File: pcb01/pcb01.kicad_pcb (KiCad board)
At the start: 2 copper layers, 118.1 x 98.4 mm, 38 parts, among them J1 DIN41612_02x32_AC, J10 Conn_01x02_Socket, J11 Conn_01x09, J2 Data Bus, J3 Address Bus, J4 Display, J5 UART, J6 UART_IRQ, J7 Jmp_Irq, J8 Jmp_NMI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

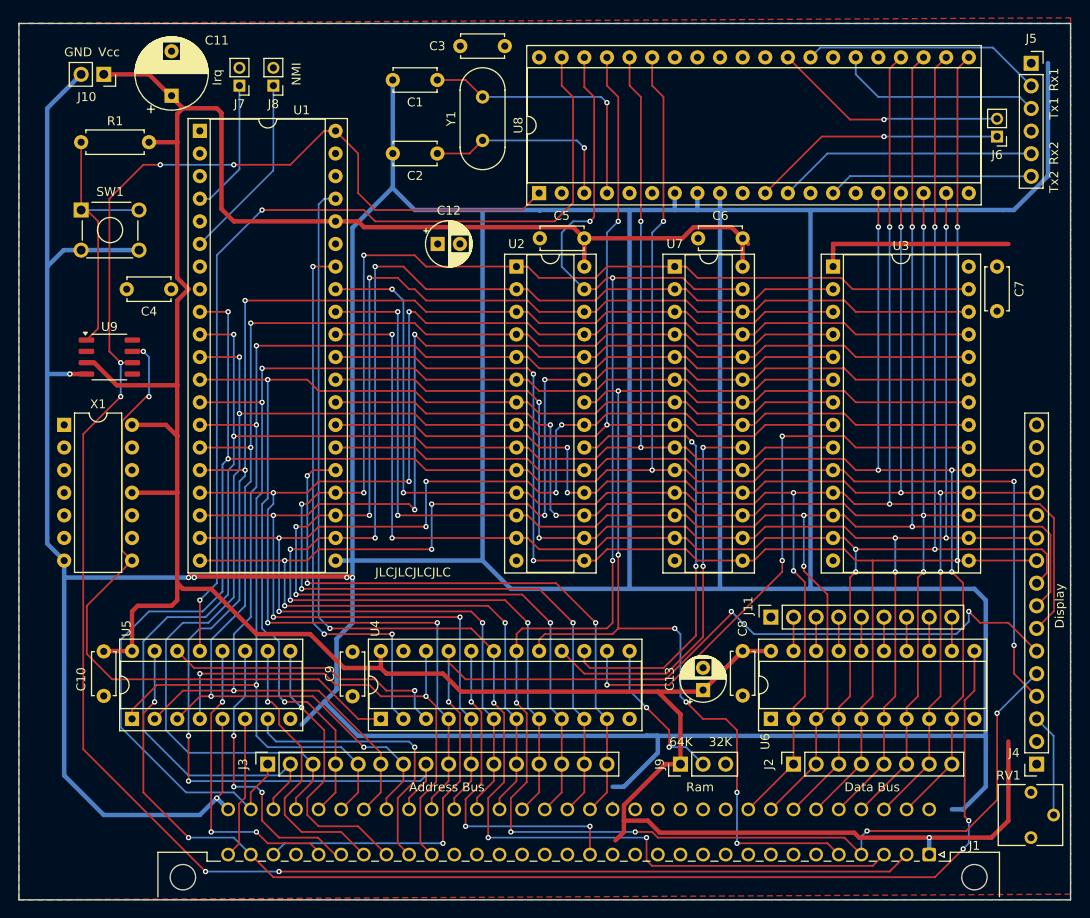
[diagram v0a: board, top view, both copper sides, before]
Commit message: add gpio00 leds
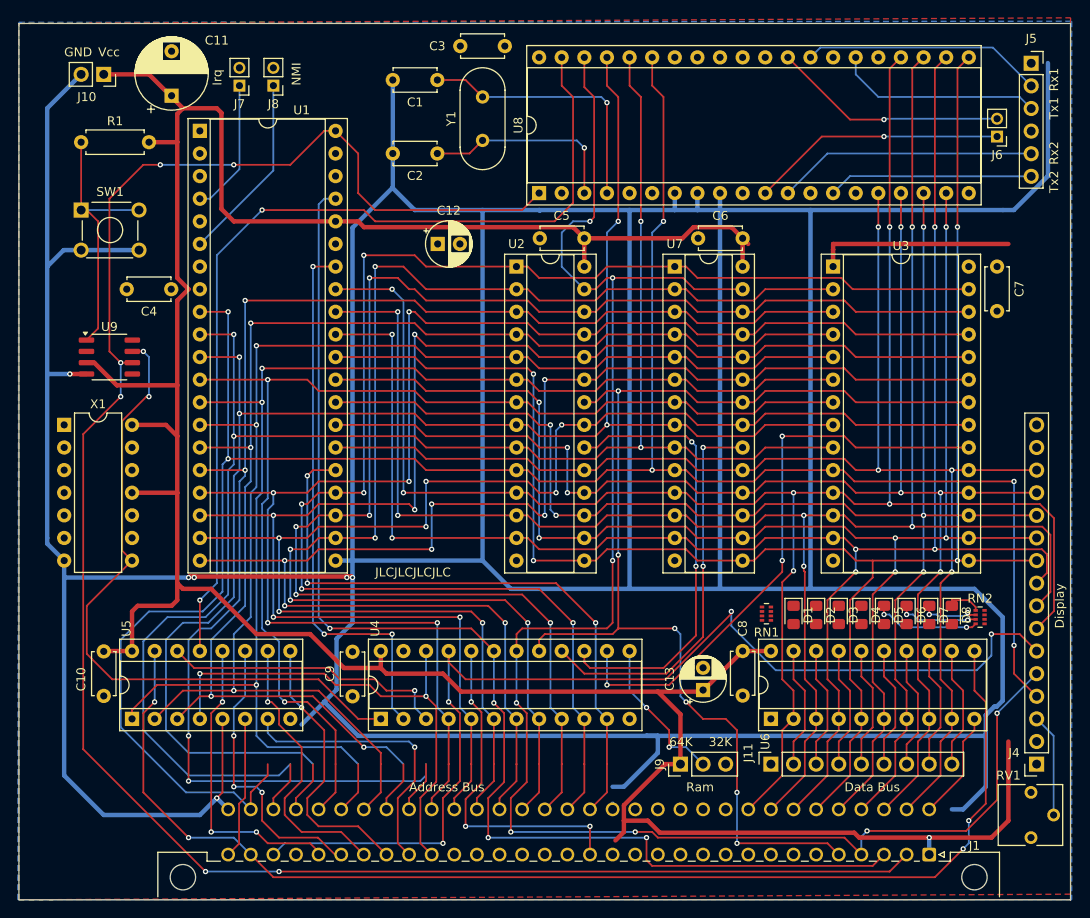
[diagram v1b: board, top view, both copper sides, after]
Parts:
- removed J2: Data Bus, Connector_PinSocket_2.54mm:PinSocket_1x08_P2.54mm_Vertical
- removed J3: Address Bus, Connector_PinSocket_2.54mm:PinSocket_1x16_P2.54mm_Vertical
- added D1: LED_Small, LED_SMD:LED_0805_2012Metric_Pad1.15x1.40mm_HandSolder, F.Cu at (108.6, 86.1)
- added D2: LED_Small, LED_SMD:LED_0805_2012Metric_Pad1.15x1.40mm_HandSolder, F.Cu at (111.1, 86.1)
- added D3: LED_Small, LED_SMD:LED_0805_2012Metric_Pad1.15x1.40mm_HandSolder, F.Cu at (113.7, 86.1)
- added D4: LED_Small, LED_SMD:LED_0805_2012Metric_Pad1.15x1.40mm_HandSolder, F.Cu at (116.2, 86.1)
- added D5: LED_Small, LED_SMD:LED_0805_2012Metric_Pad1.15x1.40mm_HandSolder, F.Cu at (118.7, 86.1)
- added D6: LED_Small, LED_SMD:LED_0805_2012Metric_Pad1.15x1.40mm_HandSolder, F.Cu at (121.3, 86.1)
- added D7: LED_Small, LED_SMD:LED_0805_2012Metric_Pad1.15x1.40mm_HandSolder, F.Cu at (123.8, 86.1)
- added D8: LED_Small, LED_SMD:LED_0805_2012Metric_Pad1.15x1.40mm_HandSolder, F.Cu at (126.4, 86.1)
- added RN1: R_Pack04, Resistor_SMD:R_Array_Concave_4x0402, F.Cu at (105.5, 86.0)
- added RN2: R_Pack04, Resistor_SMD:R_Array_Concave_4x0402, F.Cu at (129.5, 86.4)
- RV1: value R_Potentiometer_Small -> R_LCD_BIAS
- moved J11 16.5 mm to (106.0, 102.9)
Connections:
- net Net-(J11-Pin_2) renamed /GPIO00_O0
- net Net-(J11-Pin_3) renamed /GPIO00_O1
- net Net-(J11-Pin_4) renamed /GPIO00_O2
- net Net-(J11-Pin_5) renamed /GPIO00_O3
- net Net-(J11-Pin_6) renamed /GPIO00_O4
- net Net-(J11-Pin_7) renamed /GPIO00_O5
- net Net-(J11-Pin_8) renamed /GPIO00_O6
- net Net-(J11-Pin_9) renamed /GPIO00_O7
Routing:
- net GND: track 685.4 -> 699.4 mm
- net Net-(D5-K): track 0.00 -> 12.0 mm, vias 0 -> 2
- net /GPIO00_O7: track 3.81 -> 13.8 mm
- net /GPIO00_O0: track 3.81 -> 13.8 mm
- net /GPIO00_O5: track 3.81 -> 13.8 mm
- net /GPIO00_O2: track 3.81 -> 13.8 mm
- net /GPIO00_O1: track 3.81 -> 13.8 mm
- net /GPIO00_O6: track 3.81 -> 13.8 mm
- net /GPIO00_O4: track 3.81 -> 13.8 mm
- net /GPIO00_O3: track 3.81 -> 13.8 mm
- net Net-(D6-K): track 0.00 -> 9.03 mm, vias 0 -> 2
- net Net-(D7-K): track 0.00 -> 6.52 mm, vias 0 -> 2
- net Net-(D8-K): track 0.00 -> 4.01 mm
- net /DISP_EN: track 118.5 -> 121.5 mm
- net /D1: track 204.8 -> 203.7 mm
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
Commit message: wire up GPIO0 leds, adapt design rules
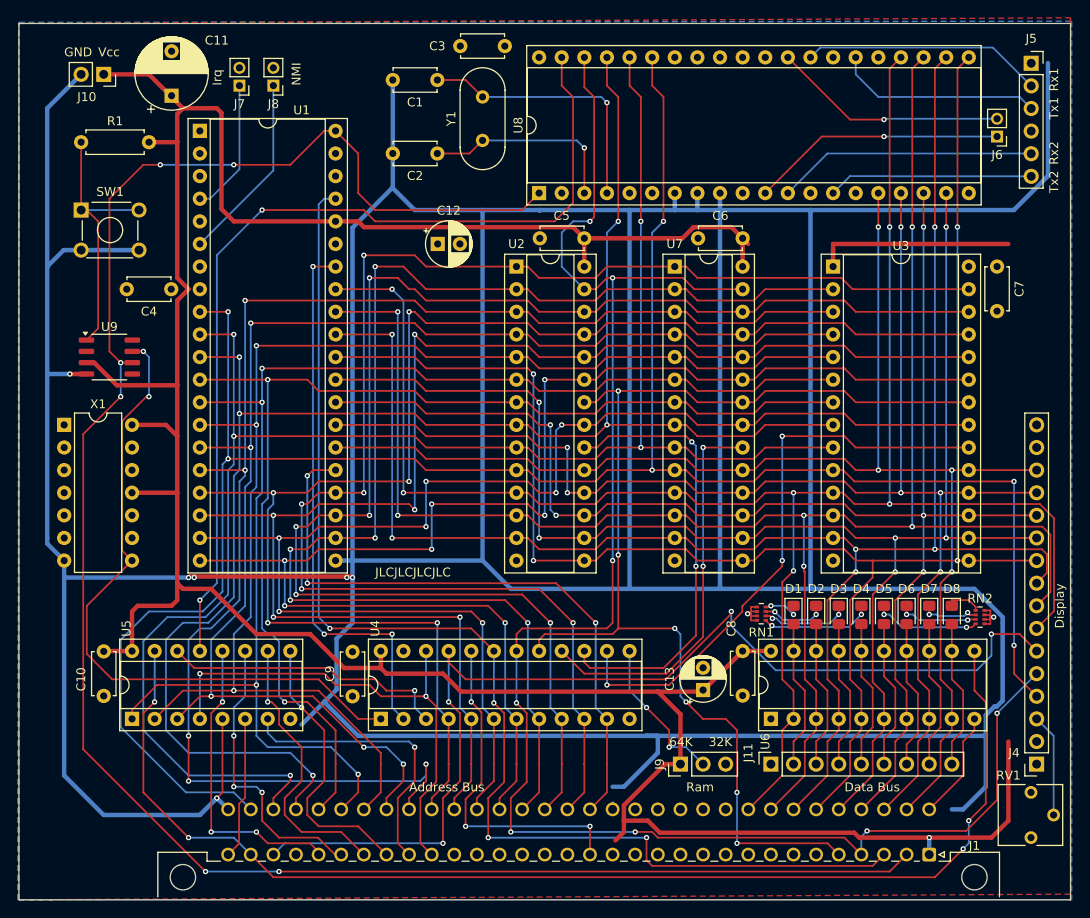
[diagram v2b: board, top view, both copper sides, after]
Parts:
- moved RN1 0.58 mm to (105.0, 86.0)
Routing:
- net Net-(D4-K): track 0.00 -> 12.6 mm, vias 0 -> 2
- net Net-(D3-K): track 0.00 -> 9.94 mm, vias 0 -> 2
- net GND: track 699.4 -> 708.4 mm, vias 6 -> 8
- net Net-(D2-K): track 0.00 -> 7.27 mm, vias 0 -> 2
- net /A0: track 246.7 -> 240.8 mm
- net Net-(D1-K): track 0.00 -> 4.56 mm, vias 0 -> 2
- net /GPIO00_O7: track 13.8 -> 16.8 mm
- net /GPIO00_O6: track 13.8 -> 16.8 mm
- net /GPIO00_O5: track 13.8 -> 16.8 mm
- net /GPIO00_O4: track 13.8 -> 16.8 mm
- net /GPIO00_O3: track 13.8 -> 16.8 mm
- net /GPIO00_O2: track 13.8 -> 16.8 mm
- net /GPIO00_O1: track 13.8 -> 16.8 mm
- net /GPIO00_O0: track 13.8 -> 16.8 mm
- net /A1: track 194.3 -> 192.5 mm, vias 4 -> 5
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
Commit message: kind of final pcb design
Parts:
- added D10: LED_Small, LED_SMD:LED_0805_2012Metric_Pad1.15x1.40mm_HandSolder, F.Cu at (86.4, 101.6)
- added D11: LED_Small, LED_SMD:LED_0805_2012Metric_Pad1.15x1.40mm_HandSolder, F.Cu at (83.8, 101.6)
- added D12: LED_Small, LED_SMD:LED_0805_2012Metric_Pad1.15x1.40mm_HandSolder, F.Cu at (81.3, 101.6)
- added D9: LED_Small, LED_SMD:LED_0805_2012Metric_Pad1.15x1.40mm_HandSolder, F.Cu at (88.9, 101.6)
- added RN3: R_Pack04, Resistor_SMD:R_Array_Concave_4x0402, B.Cu at (85.0, 105.0)
- RN1, RN2: moved to B.Cu
- moved D4 7.70 mm to (108.5, 86.1)
- moved D1 7.62 mm to (116.2, 86.1)
- moved D5 7.62 mm to (126.4, 86.1)
- moved D8 7.62 mm to (118.7, 86.1)
- moved D2 2.54 mm to (113.7, 86.1)
- moved D3 2.54 mm to (111.1, 86.1)
- moved D6 2.54 mm to (123.8, 86.1)
- moved D7 2.54 mm to (121.3, 86.1)
- moved RN2 0.64 mm to (128.9, 86.2)
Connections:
- D1 pad 2: /GPIO00_O0 -> /GPIO00_O3
- D2 pad 2: /GPIO00_O1 -> /GPIO00_O2
- D3 pad 2: /GPIO00_O2 -> /GPIO00_O1
- D4 pad 2: /GPIO00_O3 -> /GPIO00_O0
- D5 pad 2: /GPIO00_O4 -> /GPIO00_O7
- D6 pad 2: /GPIO00_O5 -> /GPIO00_O6
- D7 pad 2: /GPIO00_O6 -> /GPIO00_O5
- D8 pad 2: /GPIO00_O7 -> /GPIO00_O4
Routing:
- net /~{CS_RAM0}: track 50.4 -> 61.3 mm, vias 2 -> 3
- net /~{CS_RAM1}: track 44.3 -> 55.3 mm, vias 2 -> 3
- net Net-(D5-K): track 12.0 -> 2.30 mm, vias 2 -> 1
- net GND: track 708.4 -> 699.9 mm, vias 8 -> 6
- net Net-(D4-K): track 12.6 -> 4.44 mm, vias 2 -> 1
- net Net-(D1-K): track 4.56 -> 12.6 mm, vias 2 -> 1
- net /~{QWE_RAM}: track 197.9 -> 205.7 mm
- net /~{CS_ROM}: track 65.5 -> 72.6 mm, vias 3 -> 4
- net Net-(D8-K): track 4.01 -> 11.1 mm, vias 0 -> 1
- net Net-(D9-K): track 0.00 -> 4.58 mm, vias 0 -> 1
- net Net-(D12-K): track 0.00 -> 4.48 mm, vias 0 -> 1
- net Net-(D6-K): track 9.03 -> 5.57 mm, vias 2 -> 1
- net Net-(D10-K): track 0.00 -> 2.93 mm, vias 0 -> 1
- net Net-(D2-K): track 7.27 -> 10.0 mm, vias 2 -> 1
- net Net-(D11-K): track 0.00 -> 2.70 mm, vias 0 -> 1
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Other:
- board text added: "~{R0}"
- board text added: "~{R1}"
- board text added: "~{ROM}"
- board text added: "~{WE}"
- board text removed: "Address Bus"
- board text removed: "Data Bus"

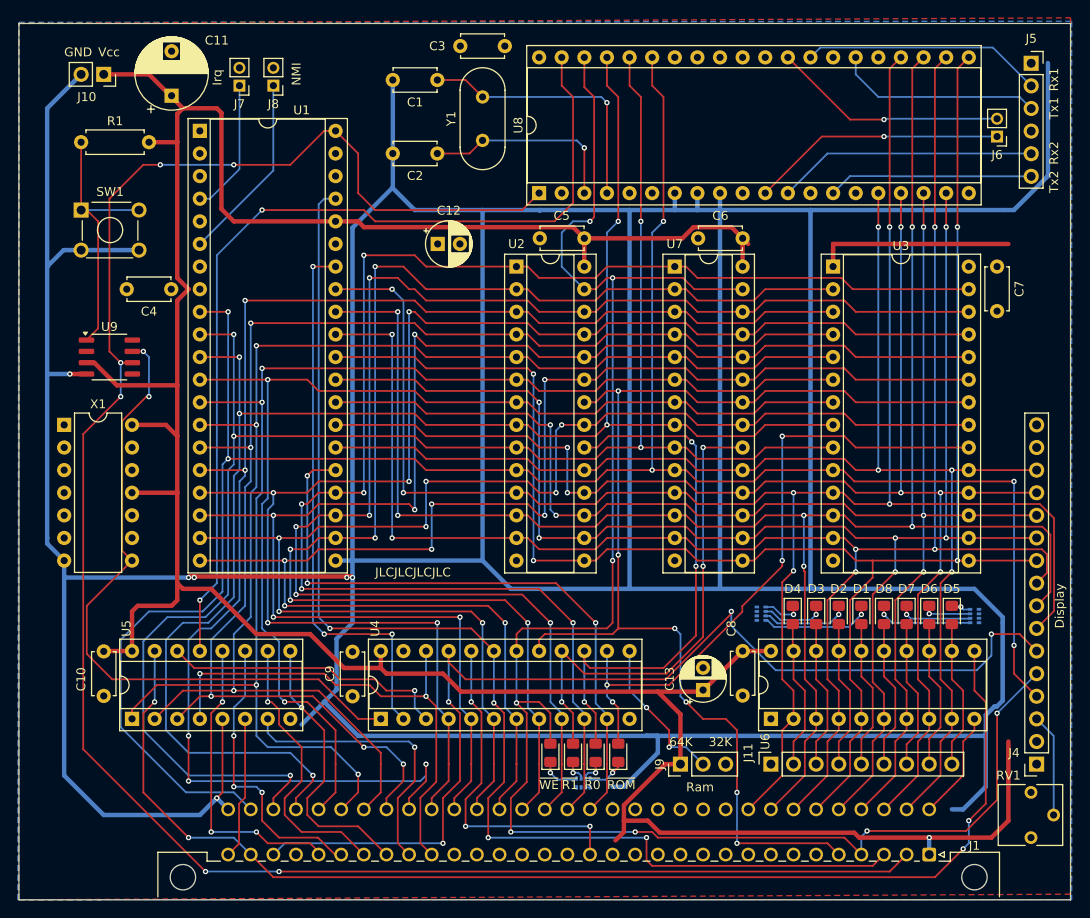
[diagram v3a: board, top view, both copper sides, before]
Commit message: fixed errors of first pcb (hopefully didn't mess up everything)
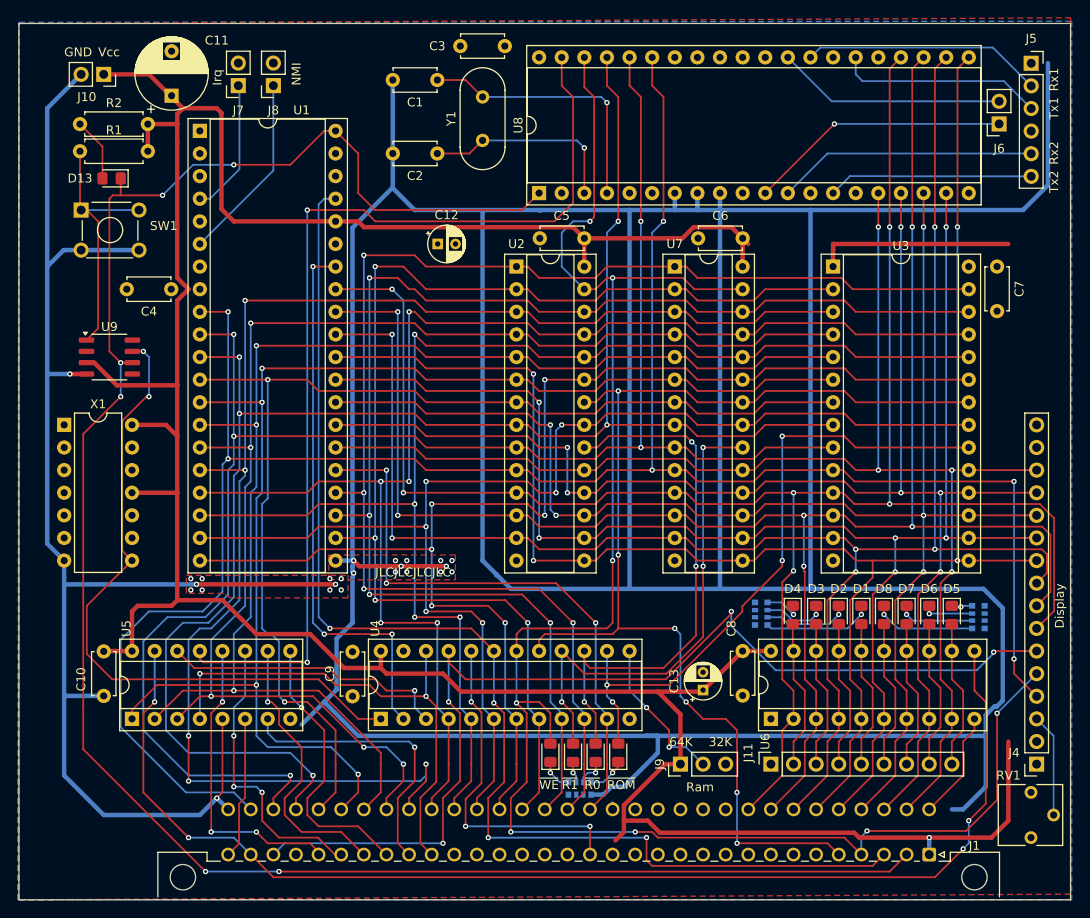
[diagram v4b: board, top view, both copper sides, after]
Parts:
- added D13: LED_Small, LED_SMD:LED_0805_2012Metric_Pad1.15x1.40mm_HandSolder, F.Cu at (32.0, 37.1)
- added R2: R, Resistor_THT:R_Axial_DIN0207_L6.3mm_D2.5mm_P7.62mm_Horizontal, F.Cu at (28.4, 31.0)
- C12, C13: footprint Capacitor_THT:CP_Radial_D5.0mm_P2.50mm -> Capacitor_THT:CP_Radial_D4.0mm_P2.00mm
- J6, J7, J8: footprint Connector_PinHeader_2.00mm:PinHeader_1x02_P2.00mm_Vertical -> Connector_PinSocket_2.54mm:PinSocket_1x02_P2.54mm_Vertical
- RN1, RN2, RN3: footprint Resistor_SMD:R_Array_Concave_4x0402 -> Resistor_SMD:R_Array_Convex_4x0612
- moved J6 1.44 mm to (131.7, 31.0)
- moved R1 1.02 mm to (28.4, 34.0)
- moved RN3 0.74 mm to (84.6, 105.6)
- moved RN2 0.45 mm to (129.3, 86.4)
- moved J7 0.13 mm to (46.2, 26.7)
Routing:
- net /A9: track 165.3 -> 149.8 mm, vias 5 -> 4
- net /A10: track 155.8 -> 140.5 mm, vias 7 -> 6
- net /A11: track 162.7 -> 147.5 mm, vias 7 -> 6
- net /A12: track 150.8 -> 137.0 mm, vias 5 -> 4
- net /A13: track 166.2 -> 154.3 mm, vias 5 -> 4
- net /A8: track 165.3 -> 153.6 mm
- net /A14: track 168.6 -> 158.6 mm, vias 5 -> 4
- net Net-(D13-A): track 0.00 -> 7.14 mm
- net /~{IOEN_02_UART}: track 105.6 -> 112.0 mm
- net /A15: track 72.0 -> 66.0 mm
- net /DISP_EN: track 121.5 -> 118.5 mm
- net VCC: track 380.0 -> 382.4 mm
- net GND: track 699.9 -> 702.1 mm, vias 6 -> 24
- net /~{RES}: track 222.8 -> 224.8 mm
- net Net-(U9-~{PB_RST}): track 30.4 -> 29.5 mm
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- added copper zone on F.Cu, net GND

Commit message: switch to top/bottom ground fill + VCC tree topology
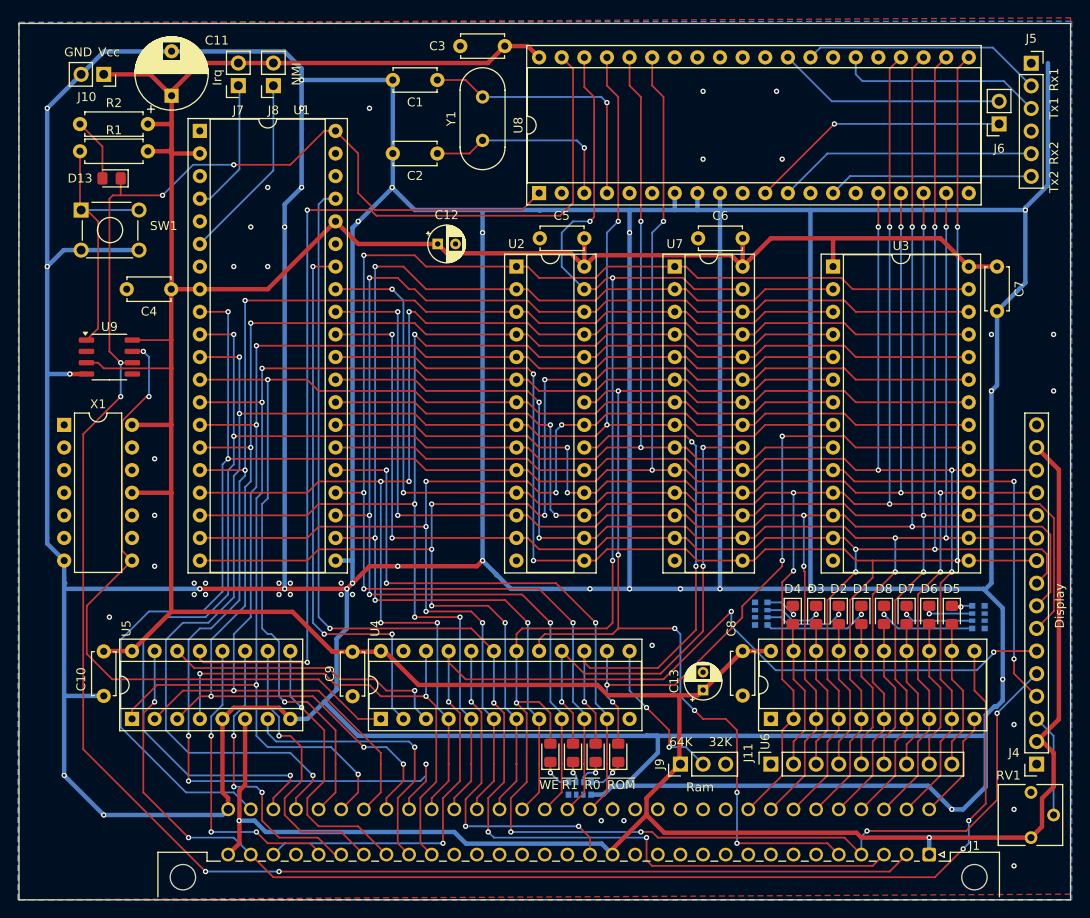
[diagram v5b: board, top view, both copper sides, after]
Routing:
- net GND: track 702.1 -> 898.4 mm, vias 24 -> 61
- net VCC: track 382.4 -> 511.5 mm, vias 1 -> 2
- net /~{SYS_CLK}: track 38.0 -> 37.3 mm
- net /~{IOEN_02_UART}: track 112.0 -> 111.5 mm
- removed copper zone on F.Cu, net VCC
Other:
- board text removed: "JLCJLCJLCJLC"
